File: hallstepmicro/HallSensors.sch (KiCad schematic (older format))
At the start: 17 parts, among them K1 CONN_3, K2 CONN_3, K3 CONN_3, K4 CONN_3

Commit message: Simplify. Simplify. Simplify.
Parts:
- removed HALL6OUT1: CONN_6, symbol CONN_6
- removed K1, K2, K3, K4: CONN_3, symbol CONN_3
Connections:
- wire segments 60 -> 52
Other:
- note removed: "Thru-holes for\nTO-92 case style."
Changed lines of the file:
@@
-EESchema Schematic File Version 2  date Monday, 30 September, 2013 11:09:14 am
+EESchema Schematic File Version 2  date Monday, 30 September, 2013 02:09:26 pm
 LIBS:power
 LIBS:device
@@
 	1    0    0    -1
 $EndComp
-$Comp
-L CONN_3 K1
-U 1 1 5246F943
-P 1700 2550
-F 0 "K1" V 1650 2550 50  0000 C CNN
-F 1 "CONN_3" V 1750 2550 40  0000 C CNN
-F 2 "" H 1700 2550 60  0000 C CNN
-F 3 "" H 1700 2550 60  0000 C CNN
-	1    1700 2550
-	0    -1   -1   0
-$EndComp
-$Comp
-L CONN_3 K2
-U 1 1 5246F952
-P 3000 2550
-F 0 "K2" V 2950 2550 50  0000 C CNN
-F 1 "CONN_3" V 3050 2550 40  0000 C CNN
-F 2 "" H 3000 2550 60  0000 C CNN
-F 3 "" H 3000 2550 60  0000 C CNN
-	1    3000 2550
-	0    -1   -1   0
-$EndComp
-$Comp
-L CONN_3 K3
-U 1 1 5246F961
-P 4300 2550
-F 0 "K3" V 4250 2550 50  0000 C CNN
-F 1 "CONN_3" V 4350 2550 40  0000 C CNN
-F 2 "" H 4300 2550 60  0000 C CNN
-F 3 "" H 4300 2550 60  0000 C CNN
-	1    4300 2550
-	0    -1   -1   0
-$EndComp
-$Comp
-L CONN_3 K4
-U 1 1 5246F970
-P 5600 2550
-F 0 "K4" V 5550 2550 50  0000 C CNN
-F 1 "CONN_3" V 5650 2550 40  0000 C CNN
-F 2 "" H 5600 2550 60  0000 C CNN
-F 3 "" H 5600 2550 60  0000 C CNN
-	1    5600 2550
-	0    -1   -1   0
-$EndComp
 Text Label 5700 3100 0    60   ~ 0
 hall4_out
@@
 Text Notes 3350 5600 0    60   ~ 0
 Enable I/O Pull-Up\nresistors on hall* inputs.
-Text Notes 4450 2300 0    60   ~ 0
-Thru-holes for\nTO-92 case style.
 Text Label 3350 5000 0    60   ~ 0
 hall1_out
@@
 Text Label 3350 5300 0    60   ~ 0
 hall4_out
-$Comp
-L CONN_6 HALL6OUT1
-U 1 1 52485994
-P 4150 5050
-F 0 "HALL6OUT1" V 4100 5050 60  0000 C CNN
-F 1 "CONN_6" V 4200 5050 60  0000 C CNN
-F 2 "" H 4150 5050 60  0000 C CNN
-F 3 "" H 4150 5050 60  0000 C CNN
-	1    4150 5050
-	1    0    0    -1
-$EndComp
-Wire Wire Line
-	4400 2900 4400 3300
 Wire Wire Line
 	5400 2400 5400 3300
@@
 Wire Wire Line
 	1500 2400 1500 3300
-Wire Wire Line
-	3100 2900 3100 3300
-Wire Wire Line
-	1800 2900 1800 3300
-Wire Wire Line
-	5700 2900 5700 3300
 Wire Wire Line
 	5200 3700 5200 3800
@@
 Connection ~ 1500 3200
 Wire Wire Line
-	1700 2900 1700 3000
-Wire Wire Line
-	3000 2900 3000 3000
-Wire Wire Line
-	4300 2900 4300 3000
-Wire Wire Line
-	5600 2900 5600 3000
-Wire Wire Line
-	1600 2900 1500 2900
-Connection ~ 1500 2900
-Wire Wire Line
-	2800 2900 2900 2900
-Connection ~ 2800 2900
-Wire Wire Line
-	4200 2900 4100 2900
-Connection ~ 4100 2900
-Wire Wire Line
-	5500 2900 5400 2900
-Connection ~ 5400 2900
-Wire Wire Line
 	3800 4800 3300 4800
 Wire Wire Line
@@
 	3800 5300 3300 5300
 $Comp
-L VCC #PWR024
+L VCC #PWR022
 U 1 1 524876B3
 P 1500 2400
-F 0 "#PWR024" H 1500 2500 30  0001 C CNN
+F 0 "#PWR022" H 1500 2500 30  0001 C CNN
 F 1 "VCC" H 1500 2500 30  0000 C CNN
 F 2 "" H 1500 2400 60  0000 C CNN
@@
 $EndComp
 $Comp
-L VCC #PWR025
+L VCC #PWR023
 U 1 1 52487795
 P 2800 2400
-F 0 "#PWR025" H 2800 2500 30  0001 C CNN
+F 0 "#PWR023" H 2800 2500 30  0001 C CNN
 F 1 "VCC" H 2800 2500 30  0000 C CNN
 F 2 "" H 2800 2400 60  0000 C CNN
@@
 $EndComp
 $Comp
-L VCC #PWR026
+L VCC #PWR024
 U 1 1 5248779B
 P 4100 2400
-F 0 "#PWR026" H 4100 2500 30  0001 C CNN
+F 0 "#PWR024" H 4100 2500 30  0001 C CNN
 F 1 "VCC" H 4100 2500 30  0000 C CNN
 F 2 "" H 4100 2400 60  0000 C CNN
@@
 $EndComp
 $Comp
-L VCC #PWR027
+L VCC #PWR025
 U 1 1 524877A1
 P 5400 2400
-F 0 "#PWR027" H 5400 2500 30  0001 C CNN
+F 0 "#PWR025" H 5400 2500 30  0001 C CNN
 F 1 "VCC" H 5400 2500 30  0000 C CNN
 F 2 "" H 5400 2400 60  0000 C CNN
@@
 $EndComp
 $Comp
-L VCC #PWR028
+L VCC #PWR026
 U 1 1 524877AD
 P 3400 4800
-F 0 "#PWR028" H 3400 4900 30  0001 C CNN
+F 0 "#PWR026" H 3400 4900 30  0001 C CNN
 F 1 "VCC" H 3400 4900 30  0000 C CNN
 F 2 "" H 3400 4800 60  0000 C CNN
@@
 $EndComp
 $Comp
-L VSS #PWR029
+L VSS #PWR027
 U 1 1 52487880
 P 1800 4100
-F 0 "#PWR029" H 1800 4100 30  0001 C CNN
+F 0 "#PWR027" H 1800 4100 30  0001 C CNN
 F 1 "VSS" H 1800 4030 30  0000 C CNN
 F 2 "" H 1800 4100 60  0000 C CNN
@@
 	5700 3700 5700 4100
 $Comp
-L VSS #PWR030
+L VSS #PWR028
 U 1 1 52487897
 P 3100 4100
-F 0 "#PWR030" H 3100 4100 30  0001 C CNN
+F 0 "#PWR028" H 3100 4100 30  0001 C CNN
 F 1 "VSS" H 3100 4030 30  0000 C CNN
 F 2 "" H 3100 4100 60  0000 C CNN
@@
 $EndComp
 $Comp
-L VSS #PWR031
+L VSS #PWR029
 U 1 1 5248789D
 P 4400 4100
-F 0 "#PWR031" H 4400 4100 30  0001 C CNN
+F 0 "#PWR029" H 4400 4100 30  0001 C CNN
 F 1 "VSS" H 4400 4030 30  0000 C CNN
 F 2 "" H 4400 4100 60  0000 C CNN
@@
 $EndComp
 $Comp
-L VSS #PWR032
+L VSS #PWR030
 U 1 1 524878A3
 P 5700 4100
-F 0 "#PWR032" H 5700 4100 30  0001 C CNN
+F 0 "#PWR030" H 5700 4100 30  0001 C CNN
 F 1 "VSS" H 5700 4030 30  0000 C CNN
 F 2 "" H 5700 4100 60  0000 C CNN
@@
 $EndComp
 $Comp
-L VSS #PWR033
+L VSS #PWR031
 U 1 1 524878AF
 P 3400 4900
-F 0 "#PWR033" H 3400 4900 30  0001 C CNN
+F 0 "#PWR031" H 3400 4900 30  0001 C CNN
 F 1 "VSS" H 3400 4830 30  0000 C CNN
 F 2 "" H 3400 4900 60  0000 C CNN
 F 3 "" H 3400 4900 60  0000 C CNN
 	1    3400 4900
-	1    0    0    -1
-$EndComp
-$Comp
-L VSS #PWR034
-U 1 1 5248798B
-P 1700 3000
-F 0 "#PWR034" H 1700 3000 30  0001 C CNN
-F 1 "VSS" H 1700 2930 30  0000 C CNN
-F 2 "" H 1700 3000 60  0000 C CNN
-F 3 "" H 1700 3000 60  0000 C CNN
-	1    1700 3000
-	1    0    0    -1
-$EndComp
-$Comp
-L VSS #PWR035
-U 1 1 52487991
-P 3000 3000
-F 0 "#PWR035" H 3000 3000 30  0001 C CNN
-F 1 "VSS" H 3000 2930 30  0000 C CNN
-F 2 "" H 3000 3000 60  0000 C CNN
-F 3 "" H 3000 3000 60  0000 C CNN
-	1    3000 3000
-	1    0    0    -1
-$EndComp
-$Comp
-L VSS #PWR036
-U 1 1 52487997
-P 4300 3000
-F 0 "#PWR036" H 4300 3000 30  0001 C CNN
-F 1 "VSS" H 4300 2930 30  0000 C CNN
-F 2 "" H 4300 3000 60  0000 C CNN
-F 3 "" H 4300 3000 60  0000 C CNN
-	1    4300 3000
-	1    0    0    -1
-$EndComp
-$Comp
-L VSS #PWR037
-U 1 1 5248799D
-P 5600 3000
-F 0 "#PWR037" H 5600 3000 30  0001 C CNN
-F 1 "VSS" H 5600 2930 30  0000 C CNN
-F 2 "" H 5600 3000 60  0000 C CNN
-F 3 "" H 5600 3000 60  0000 C CNN
-	1    5600 3000
 	1    0    0    -1
 $EndComp
@@
 hall4
 $Comp
-L VCC #PWR038
+L VCC #PWR032
 U 1 1 5248ACFC
 P 5100 4700
-F 0 "#PWR038" H 5100 4800 30  0001 C CNN
+F 0 "#PWR032" H 5100 4800 30  0001 C CNN
 F 1 "VCC" H 5100 4800 30  0000 C CNN
 F 2 "" H 5100 4700 60  0000 C CNN
@@
 $EndComp
 $Comp
-L VSS #PWR039
+L VSS #PWR033
 U 1 1 5248AD02
 P 5100 5600
-F 0 "#PWR039" H 5100 5600 30  0001 C CNN
+F 0 "#PWR033" H 5100 5600 30  0001 C CNN
 F 1 "VSS" H 5100 5530 30  0000 C CNN
 F 2 "" H 5100 5600 60  0000 C CNN
@@
 $EndComp
 $Comp
-L PWR_FLAG #FLG040
+L PWR_FLAG #FLG034
 U 1 1 5248AD0A
 P 5100 5400
-F 0 "#FLG040" H 5100 5495 30  0001 C CNN
+F 0 "#FLG034" H 5100 5495 30  0001 C CNN
 F 1 "PWR_FLAG" H 5100 5580 30  0000 C CNN
 F 2 "" H 5100 5400 60  0000 C CNN
@@
 $EndComp
 $Comp
-L PWR_FLAG #FLG041
+L PWR_FLAG #FLG035
 U 1 1 5248AD19
 P 5100 4900
-F 0 "#FLG041" H 5100 4995 30  0001 C CNN
+F 0 "#FLG035" H 5100 4995 30  0001 C CNN
 F 1 "PWR_FLAG" H 5100 5080 30  0000 C CNN
 F 2 "" H 5100 4900 60  0000 C CNN
@@
 Wire Wire Line
 	5100 5400 5100 5600
+Wire Wire Line
+	1800 3300 1800 2900
+Wire Wire Line
+	5700 3300 5700 2900
+Wire Wire Line
+	4400 3300 4400 2900
+Wire Wire Line
+	3100 3300 3100 2900
 $EndSCHEMATC

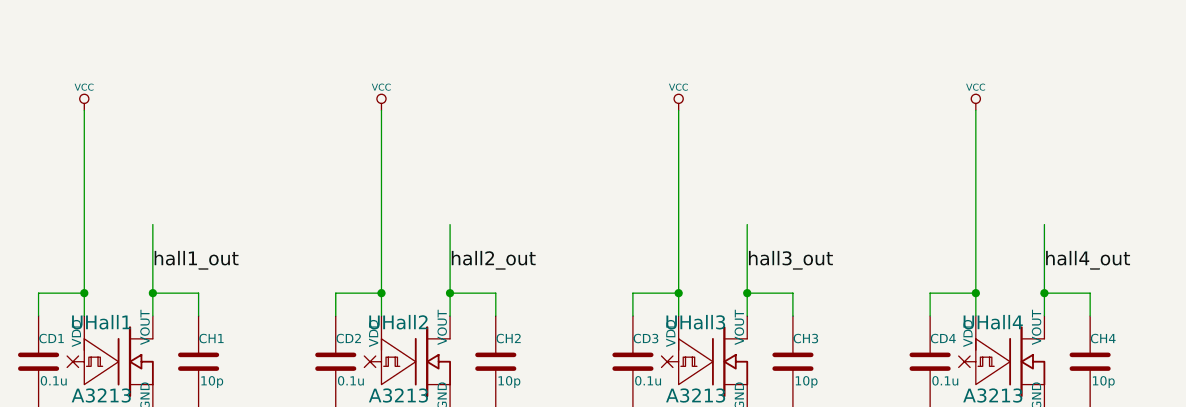
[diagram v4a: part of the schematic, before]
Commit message: Added optional pullup resistors to sensor board.
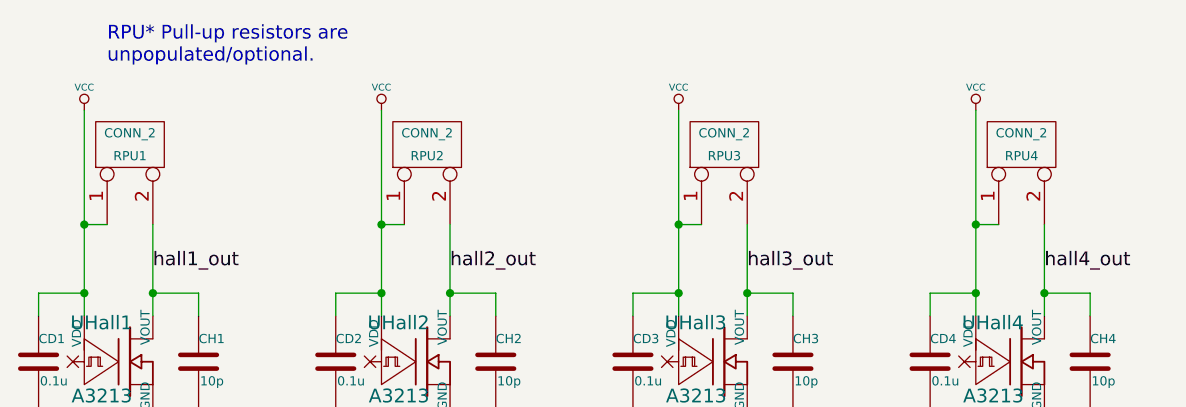
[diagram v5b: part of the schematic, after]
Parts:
- added RPU1, RPU2, RPU3, RPU4: CONN_2, symbol CONN_2
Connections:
- wire segments 52 -> 56
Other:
- note added: "RPU* Pull-up resistors are\nunpopulated/optional."
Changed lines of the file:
@@
-EESchema Schematic File Version 2  date Tuesday, 01 October, 2013 02:42:25 pm
+EESchema Schematic File Version 2  date Wednesday, 02 October, 2013 09:18:38 pm
 LIBS:power
 LIBS:device
@@
 Sheet 2 2
 Title ""
-Date "1 oct 2013"
+Date "3 oct 2013"
 Rev ""
 Comp ""
@@
 Text Label 3350 5300 0    60   ~ 0
 hall4_out
-Wire Wire Line
-	5400 2400 5400 3300
-Wire Wire Line
-	4100 2400 4100 3300
-Wire Wire Line
-	2800 2400 2800 3300
-Wire Wire Line
-	1500 2400 1500 3300
-Wire Wire Line
-	5200 3700 5200 3800
-Wire Wire Line
-	5200 3800 5700 3800
-Connection ~ 5700 3800
-Wire Wire Line
-	5200 3300 5200 3200
-Wire Wire Line
-	5200 3200 5400 3200
-Connection ~ 5400 3200
-Wire Wire Line
-	5900 3700 5900 3900
-Wire Wire Line
-	5900 3900 5700 3900
-Connection ~ 5700 3900
-Wire Wire Line
-	5900 3300 5900 3200
-Wire Wire Line
-	5900 3200 5700 3200
-Connection ~ 5700 3200
-Wire Wire Line
-	4600 3200 4600 3300
-Wire Wire Line
-	4600 3200 4400 3200
-Connection ~ 4400 3200
-Wire Wire Line
-	4600 3700 4600 3900
-Wire Wire Line
-	4600 3900 4400 3900
-Connection ~ 4400 3900
-Wire Wire Line
-	3900 3700 3900 3800
-Wire Wire Line
-	3900 3800 4400 3800
-Connection ~ 4400 3800
-Wire Wire Line
-	3900 3300 3900 3200
-Wire Wire Line
-	3900 3200 4100 3200
-Connection ~ 4100 3200
-Wire Wire Line
-	3300 3300 3300 3200
-Wire Wire Line
-	3300 3200 3100 3200
-Connection ~ 3100 3200
-Wire Wire Line
-	3300 3700 3300 3900
-Wire Wire Line
-	3300 3900 3100 3900
-Connection ~ 3100 3900
-Wire Wire Line
-	3100 3800 2600 3800
-Wire Wire Line
-	2600 3800 2600 3700
-Connection ~ 3100 3800
-Wire Wire Line
-	2600 3300 2600 3200
-Wire Wire Line
-	2600 3200 2800 3200
-Connection ~ 2800 3200
-Wire Wire Line
-	2000 3300 2000 3200
-Wire Wire Line
-	2000 3200 1800 3200
-Connection ~ 1800 3200
-Wire Wire Line
-	2000 3700 2000 3900
-Wire Wire Line
-	2000 3900 1800 3900
-Connection ~ 1800 3900
-Wire Wire Line
-	1800 3800 1300 3800
-Wire Wire Line
-	1300 3800 1300 3700
-Connection ~ 1800 3800
-Wire Wire Line
-	1300 3300 1300 3200
-Wire Wire Line
-	1300 3200 1500 3200
-Connection ~ 1500 3200
-Wire Wire Line
-	3800 4800 3300 4800
-Wire Wire Line
-	3800 4900 3300 4900
-Wire Wire Line
-	3300 5000 3800 5000
-Wire Wire Line
-	3800 5100 3300 5100
-Wire Wire Line
-	3800 5200 3300 5200
-Wire Wire Line
-	3800 5300 3300 5300
 $Comp
 L VCC #PWR022
@@
 	1    0    0    -1
 $EndComp
-Wire Wire Line
-	1800 3700 1800 4100
-Wire Wire Line
-	3100 3700 3100 4100
-Wire Wire Line
-	4400 3700 4400 4100
-Wire Wire Line
-	5700 3700 5700 4100
 $Comp
 L VSS #PWR028
@@
 	-1   0    0    1
 $EndComp
+$Comp
+L CONN_2 RPU1
+U 1 1 524CC8C3
+P 1700 2550
+F 0 "RPU1" V 1650 2550 40  0000 C CNN
+F 1 "CONN_2" V 1750 2550 40  0000 C CNN
+F 2 "" H 1700 2550 60  0000 C CNN
+F 3 "" H 1700 2550 60  0000 C CNN
+	1    1700 2550
+	0    -1   -1   0
+$EndComp
+$Comp
+L CONN_2 RPU2
+U 1 1 524CC8D2
+P 3000 2550
+F 0 "RPU2" V 2950 2550 40  0000 C CNN
+F 1 "CONN_2" V 3050 2550 40  0000 C CNN
+F 2 "" H 3000 2550 60  0000 C CNN
+F 3 "" H 3000 2550 60  0000 C CNN
+	1    3000 2550
+	0    -1   -1   0
+$EndComp
+$Comp
+L CONN_2 RPU3
+U 1 1 524CC8E1
+P 4300 2550
+F 0 "RPU3" V 4250 2550 40  0000 C CNN
+F 1 "CONN_2" V 4350 2550 40  0000 C CNN
+F 2 "" H 4300 2550 60  0000 C CNN
+F 3 "" H 4300 2550 60  0000 C CNN
+	1    4300 2550
+	0    -1   -1   0
+$EndComp
+$Comp
+L CONN_2 RPU4
+U 1 1 524CC8F0
+P 5600 2550
+F 0 "RPU4" V 5550 2550 40  0000 C CNN
+F 1 "CONN_2" V 5650 2550 40  0000 C CNN
+F 2 "" H 5600 2550 60  0000 C CNN
+F 3 "" H 5600 2550 60  0000 C CNN
+	1    5600 2550
+	0    -1   -1   0
+$EndComp
+Wire Wire Line
+	5400 2400 5400 3300
+Wire Wire Line
+	4100 2400 4100 3300
+Wire Wire Line
+	2800 2400 2800 3300
+Wire Wire Line
+	1500 2400 1500 3300
+Wire Wire Line
+	5200 3700 5200 3800
+Wire Wire Line
+	5200 3800 5700 3800
+Connection ~ 5700 3800
+Wire Wire Line
+	5200 3300 5200 3200
+Wire Wire Line
+	5200 3200 5400 3200
+Connection ~ 5400 3200
+Wire Wire Line
+	5900 3700 5900 3900
+Wire Wire Line
+	5900 3900 5700 3900
+Connection ~ 5700 3900
+Wire Wire Line
+	5900 3300 5900 3200
+Wire Wire Line
+	5900 3200 5700 3200
+Connection ~ 5700 3200
+Wire Wire Line
+	4600 3200 4600 3300
+Wire Wire Line
+	4600 3200 4400 3200
+Connection ~ 4400 3200
+Wire Wire Line
+	4600 3700 4600 3900
+Wire Wire Line
+	4600 3900 4400 3900
+Connection ~ 4400 3900
+Wire Wire Line
+	3900 3700 3900 3800
+Wire Wire Line
+	3900 3800 4400 3800
+Connection ~ 4400 3800
+Wire Wire Line
+	3900 3300 3900 3200
+Wire Wire Line
+	3900 3200 4100 3200
+Connection ~ 4100 3200
+Wire Wire Line
+	3300 3300 3300 3200
+Wire Wire Line
+	3300 3200 3100 3200
+Connection ~ 3100 3200
+Wire Wire Line
+	3300 3700 3300 3900
+Wire Wire Line
+	3300 3900 3100 3900
+Connection ~ 3100 3900
+Wire Wire Line
+	3100 3800 2600 3800
+Wire Wire Line
+	2600 3800 2600 3700
+Connection ~ 3100 3800
+Wire Wire Line
+	2600 3300 2600 3200
+Wire Wire Line
+	2600 3200 2800 3200
+Connection ~ 2800 3200
+Wire Wire Line
+	2000 3300 2000 3200
+Wire Wire Line
+	2000 3200 1800 3200
+Connection ~ 1800 3200
+Wire Wire Line
+	2000 3700 2000 3900
+Wire Wire Line
+	2000 3900 1800 3900
+Connection ~ 1800 3900
+Wire Wire Line
+	1800 3800 1300 3800
+Wire Wire Line
+	1300 3800 1300 3700
+Connection ~ 1800 3800
+Wire Wire Line
+	1300 3300 1300 3200
+Wire Wire Line
+	1300 3200 1500 3200
+Connection ~ 1500 3200
+Wire Wire Line
+	3800 4800 3300 4800
+Wire Wire Line
+	3800 4900 3300 4900
+Wire Wire Line
+	3300 5000 3800 5000
+Wire Wire Line
+	3800 5100 3300 5100
+Wire Wire Line
+	3800 5200 3300 5200
+Wire Wire Line
+	3800 5300 3300 5300
+Wire Wire Line
+	1800 3700 1800 4100
+Wire Wire Line
+	3100 3700 3100 4100
+Wire Wire Line
+	4400 3700 4400 4100
+Wire Wire Line
+	5700 3700 5700 4100
 Wire Wire Line
 	5100 4700 5100 4900
@@
 Wire Wire Line
 	3100 3300 3100 2900
+Wire Wire Line
+	1600 2900 1500 2900
+Connection ~ 1500 2900
+Wire Wire Line
+	2900 2900 2800 2900
+Connection ~ 2800 2900
+Wire Wire Line
+	4200 2900 4100 2900
+Connection ~ 4100 2900
+Wire Wire Line
+	5500 2900 5400 2900
+Connection ~ 5400 2900
+Text Notes 1600 2200 0    60   ~ 0
+RPU* Pull-up resistors are\nunpopulated/optional.
 $EndSCHEMATC
